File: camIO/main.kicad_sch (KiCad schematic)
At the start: 30 parts, among them J6 MISC, J8 CSI/DSI, Q1 BSS138, U1 PCA9306

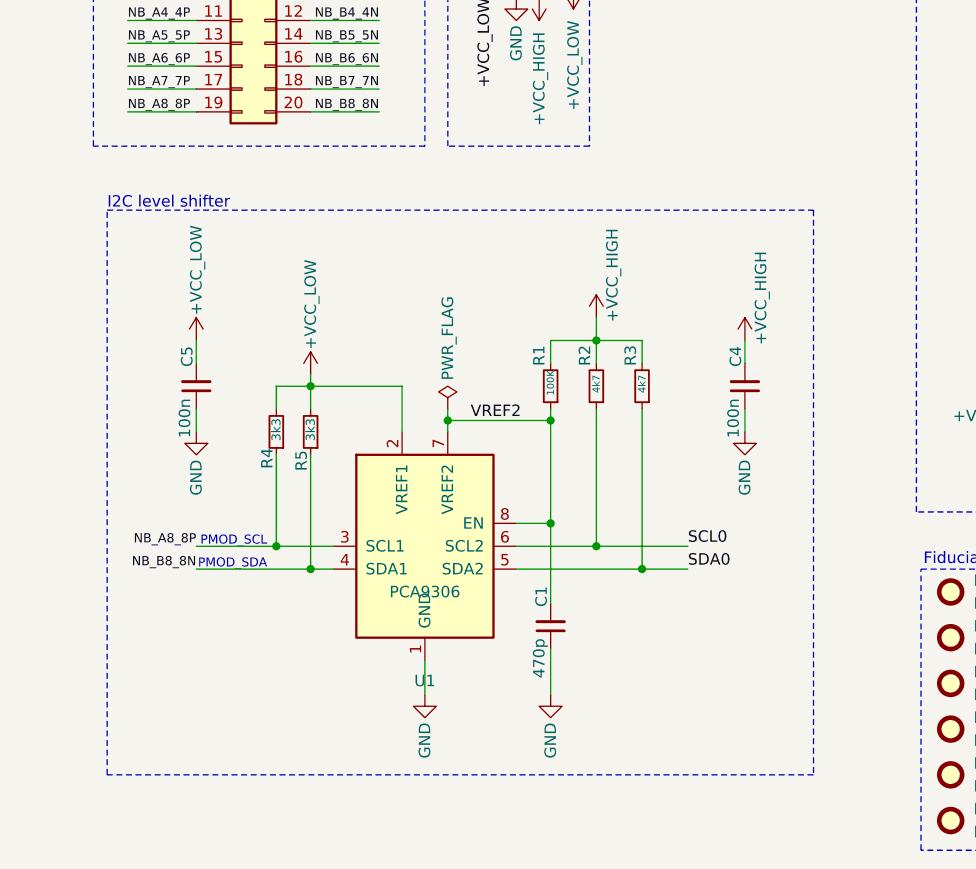
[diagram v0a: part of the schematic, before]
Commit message: Removing U1 as it is not needed - #4
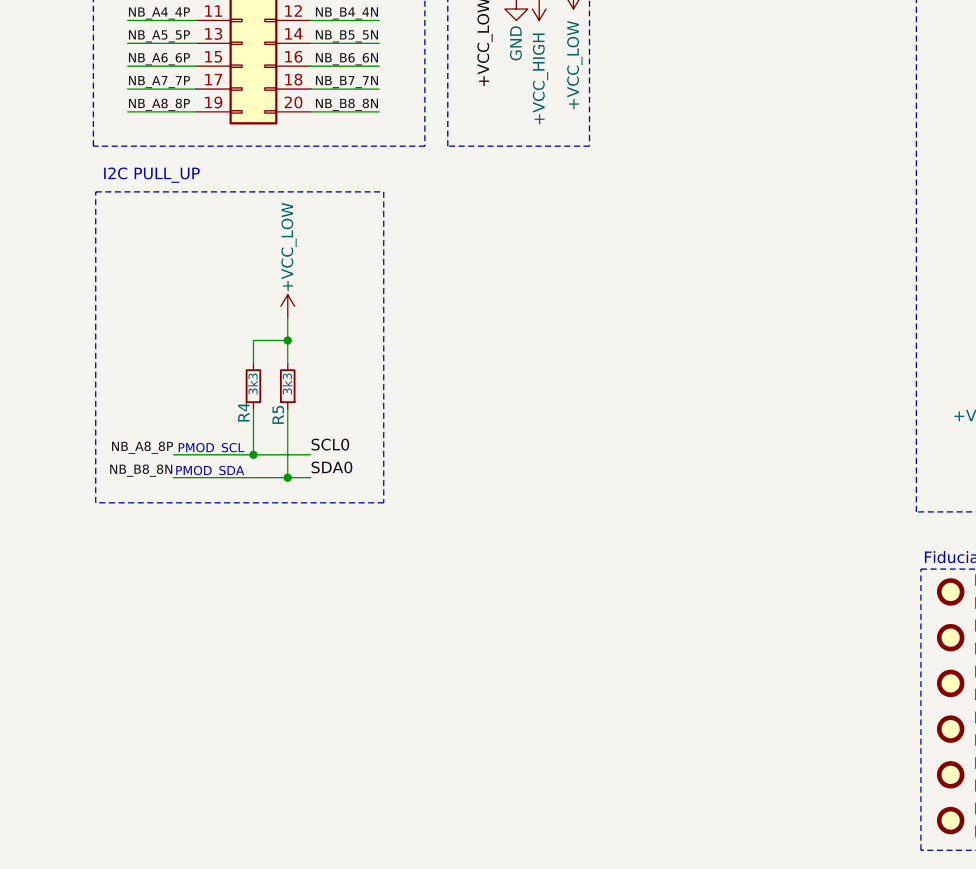
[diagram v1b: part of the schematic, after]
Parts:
- removed C1: 470p, Capacitor_SMD:C_0402_1005Metric, symbol Device:C_Small
- removed C4, C5: 100n, Capacitor_SMD:C_0402_1005Metric, symbol Device:C_Small
- removed R1: 100K, Resistor_SMD:R_0402_1005Metric, symbol Device:R_Small
- removed R2, R3: 4k7, Resistor_SMD:R_0402_1005Metric, symbol Device:R_Small
- removed U1: PCA9306, Package_SO:SSOP-8_2.95x2.8mm_P0.65mm, symbol Interface:PCA9306
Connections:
- net SCL0 is gone; now on net NB_A8_8P: J8.3 (Pin_3)
- net SDA0 is gone; now on net NB_B8_8N: J8.2 (Pin_2)
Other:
- note added: "I2C PULL_UP"
- note removed: "I2C level shifter"
- moved on the sheet: R4, R5

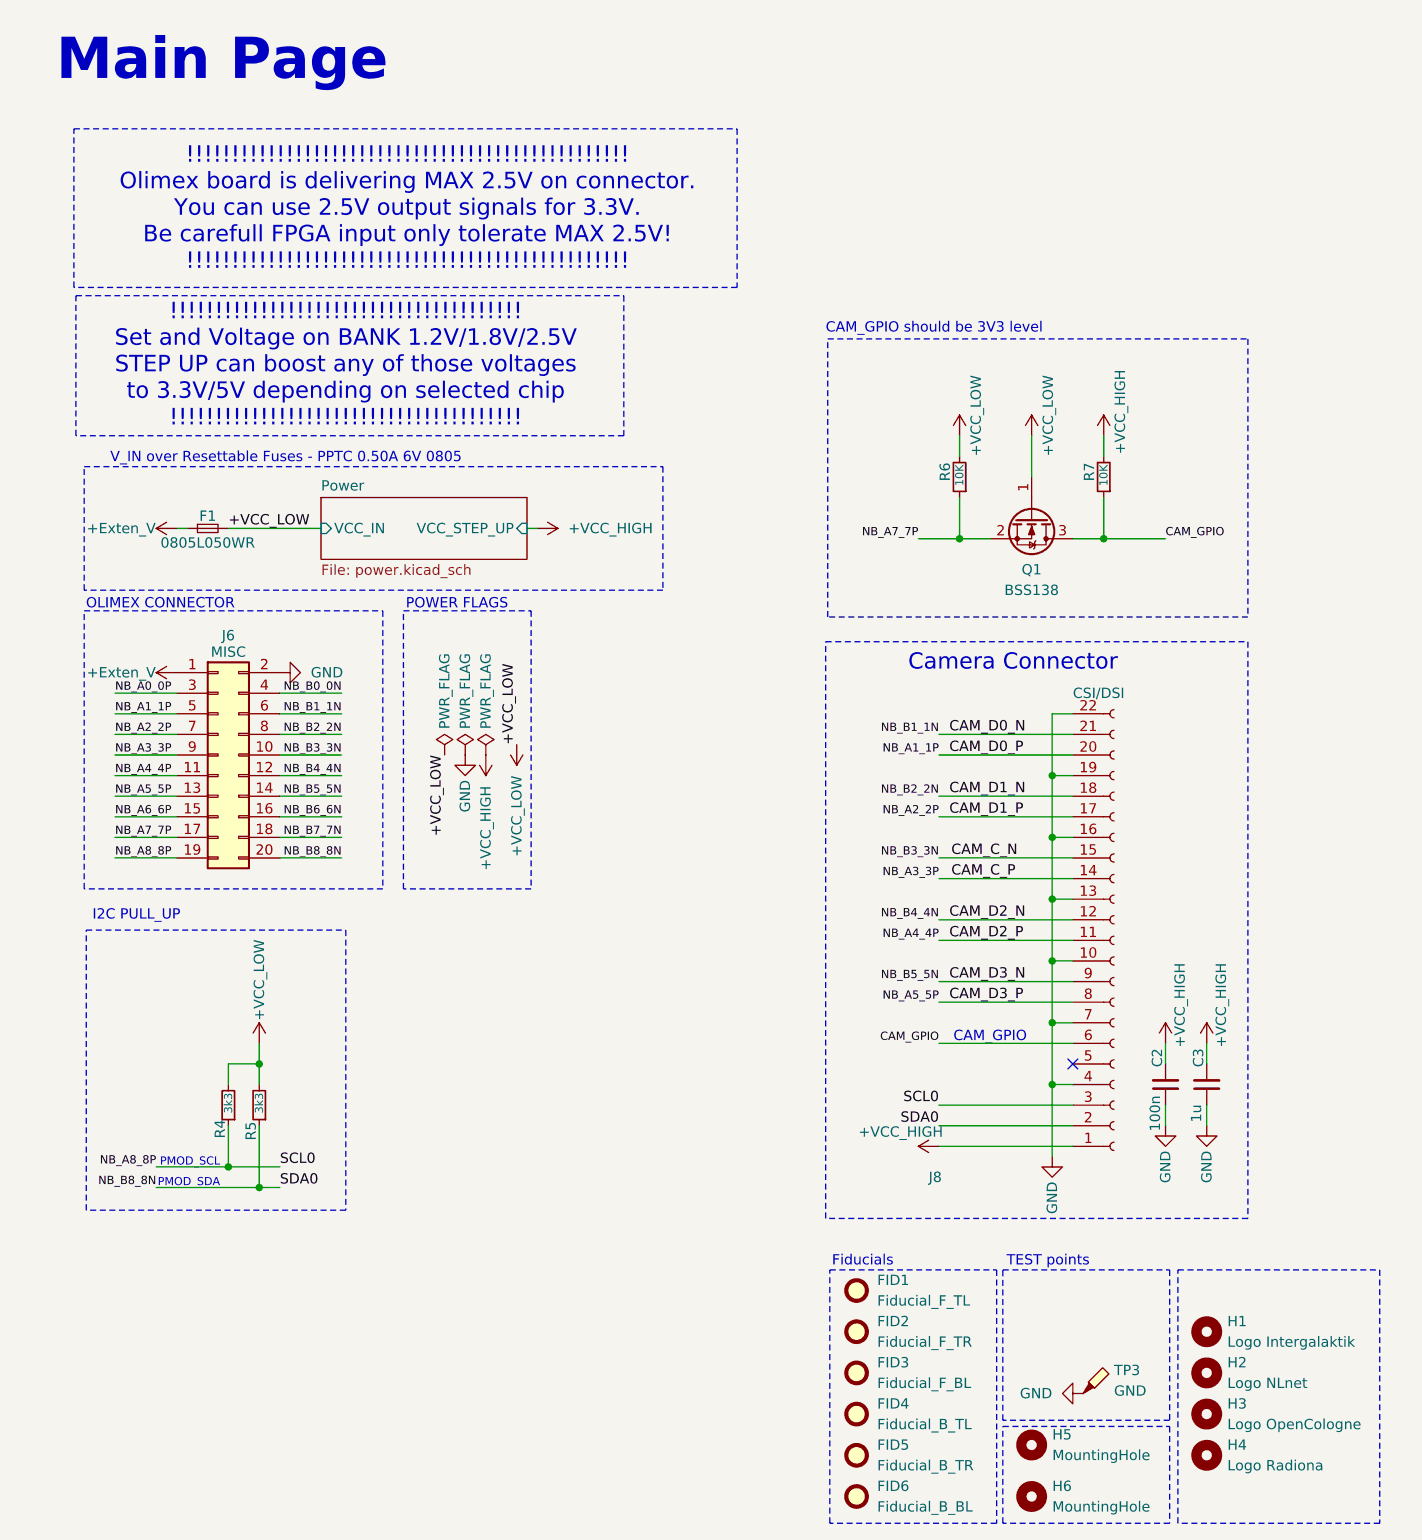
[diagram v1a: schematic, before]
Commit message: sch cleanup - reference cleanup
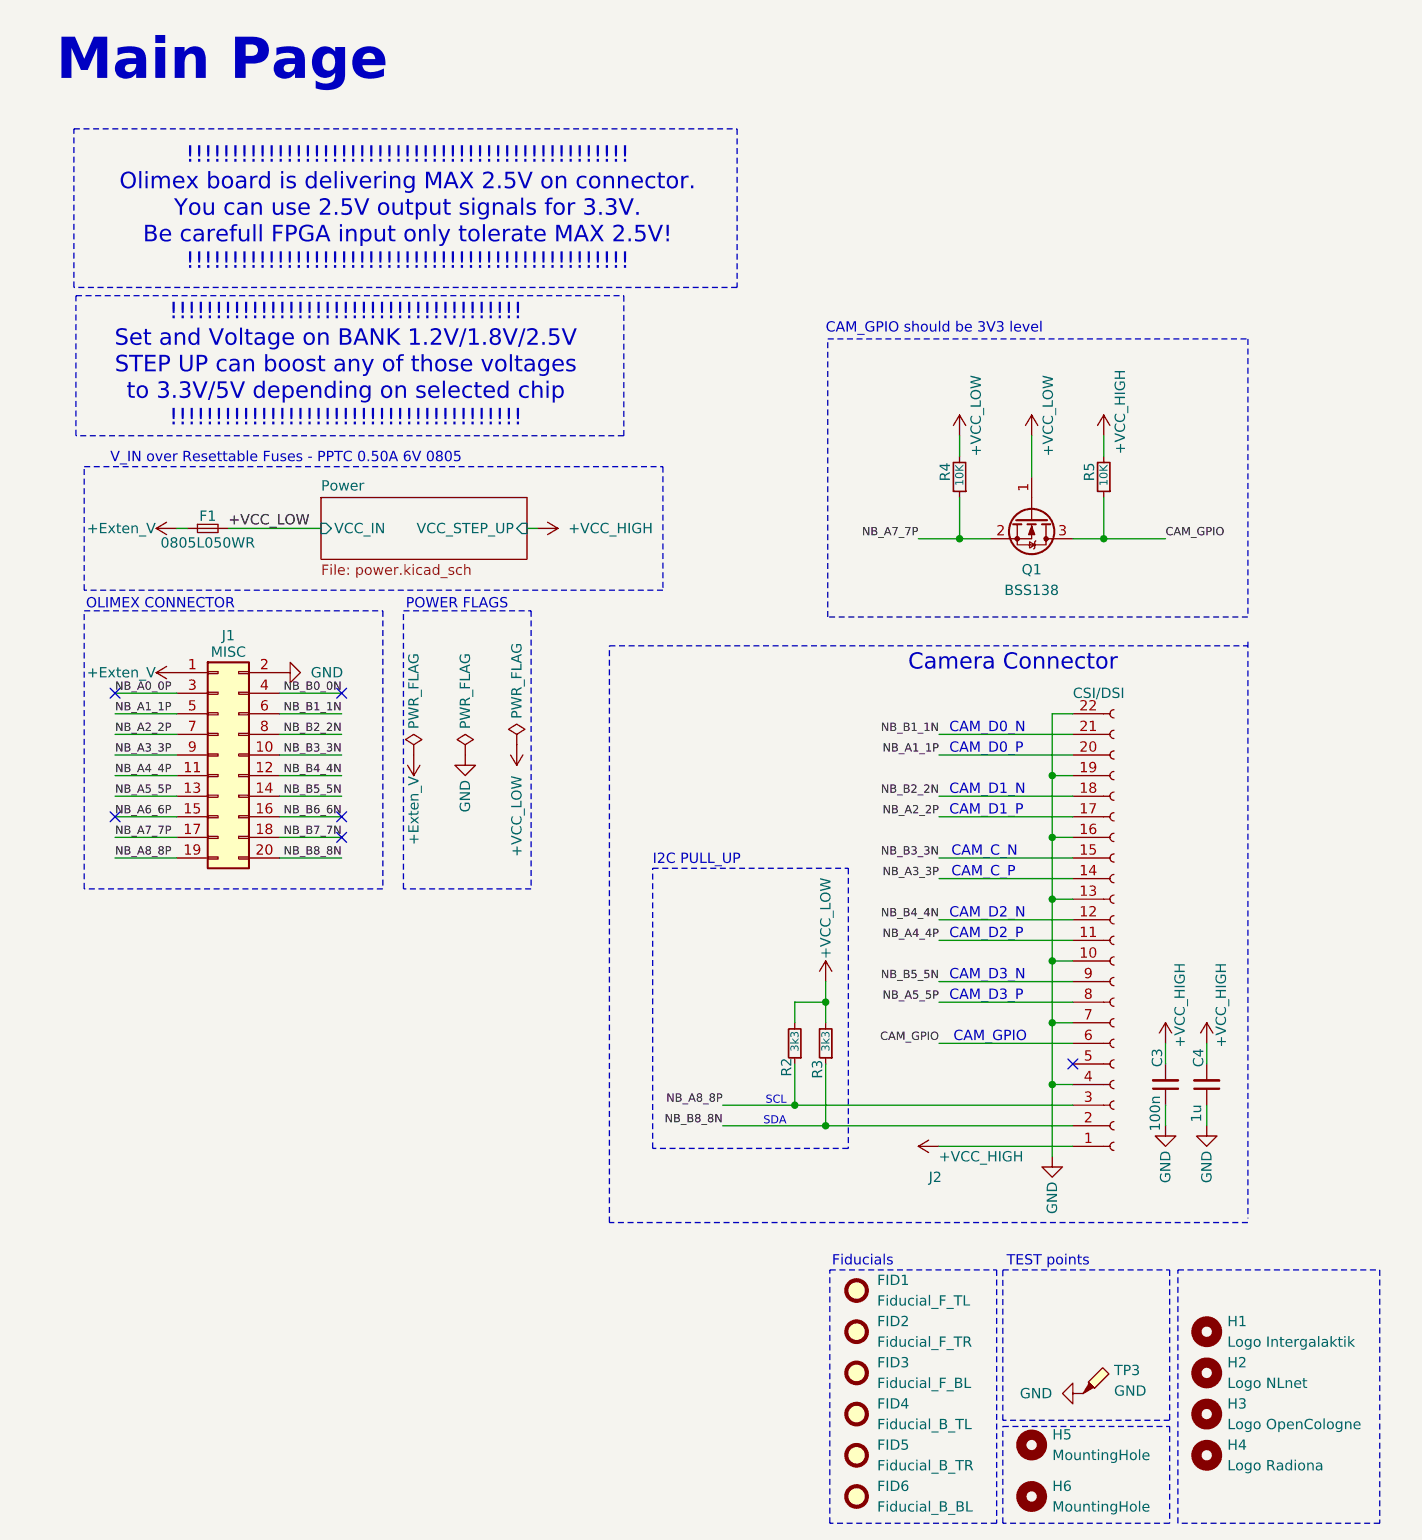
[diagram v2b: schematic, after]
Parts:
- J2: renamed from J8; symbol Connector:Conn_01x22_Female -> Connector:Conn_01x22_Socket
- renumbered C2 to C3, C3 to C4, J6 to J1, R4 to R2, R5 to R3, R6 to R4, R7 to R5
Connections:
- net CAM_C_N renamed NB_B3_3N
- net CAM_C_P renamed NB_A3_3P
- net CAM_D0_N renamed NB_B1_1N
- net CAM_D0_P renamed NB_A1_1P
- net CAM_D1_N renamed NB_B2_2N
- net CAM_D1_P renamed NB_A2_2P
- net CAM_D2_N renamed NB_B4_4N
- net CAM_D2_P renamed NB_A4_4P
- net CAM_D3_N renamed NB_B5_5N
- net CAM_D3_P renamed NB_A5_5P
- no-connect marks 1 -> 6
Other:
- note added: "CAM_C_N"
- note added: "CAM_C_P"
- note added: "CAM_D0_N"
- note added: "CAM_D0_P"
- note added: "CAM_D1_N"
- note added: "CAM_D1_P"
- note added: "CAM_D2_N"
- note added: "CAM_D2_P"
- note added: "CAM_D3_N"
- note added: "CAM_D3_P"
- note added: "SCL"
- note added: "SDA"
- note removed: "PMOD_SCL"
- note removed: "PMOD_SDA"
- moved on the sheet: R2, R3

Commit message: Adding LP pins on P side of diff pair #4
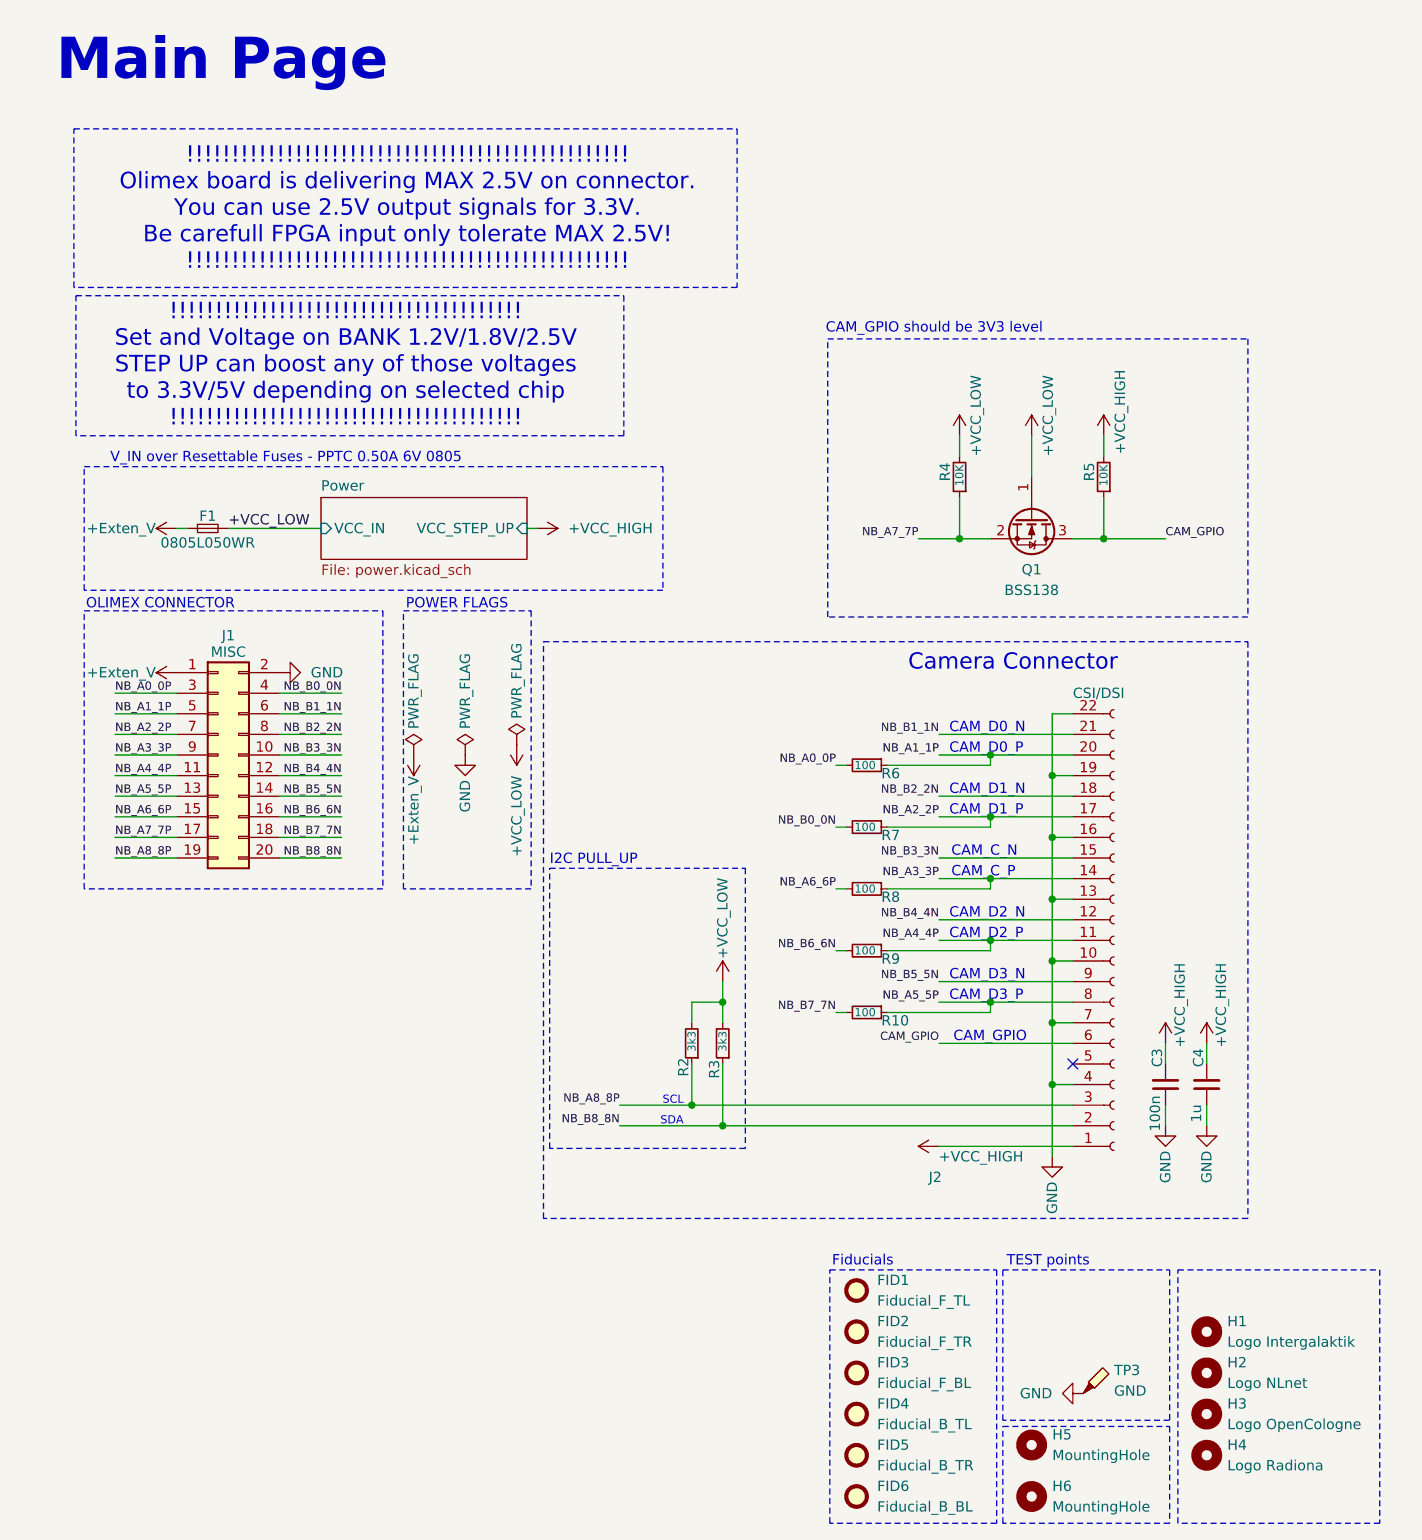
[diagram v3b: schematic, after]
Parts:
- added R10, R6, R7, R8, R9: 100, Resistor_SMD:R_0402_1005Metric, symbol Device:R_Small
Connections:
- net NB_A0_0P: now also R6.2
- net NB_A1_1P: now also R6.1
- net NB_A2_2P: now also R7.1
- net NB_A3_3P: now also R8.1
- net NB_A4_4P: now also R9.1
- net NB_A5_5P: now also R10.1
- net NB_A6_6P: now also R8.2
- net NB_B0_0N: now also R7.2
- net NB_B6_6N: now also R9.2
- net NB_B7_7N: now also R10.2
- no-connect marks 6 -> 1
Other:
- moved on the sheet: R2, R3
